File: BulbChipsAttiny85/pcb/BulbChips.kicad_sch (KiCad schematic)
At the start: 27 parts, among them J1 USB_C_Receptacle_USB2.0_14P, SW1 SW_Push, U1 DMN52D0UV, U2 USBLC6-2P6, U3 S-82A1ACA-I6T1U, U4 ATtiny85-20M, U5 BQ24045DSQR

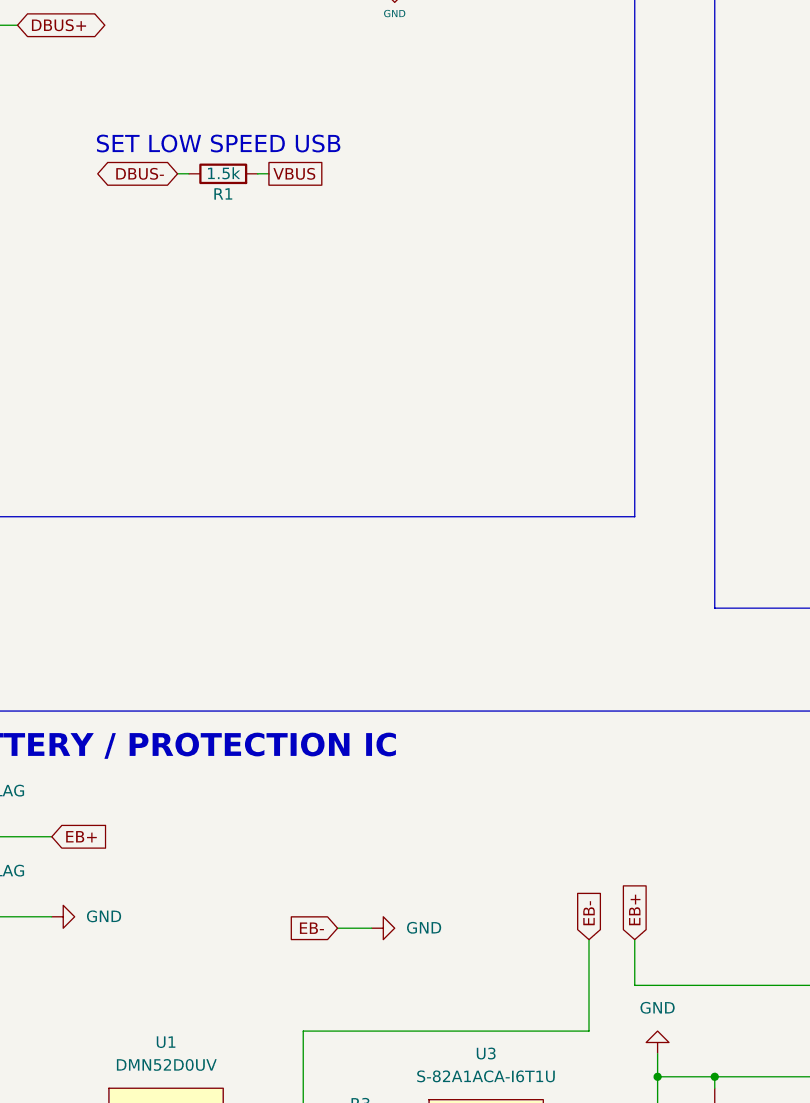
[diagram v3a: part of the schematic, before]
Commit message: changed usb low speed resistor from 1.5k to 2.2k because using 5v from usb, not 3.3v
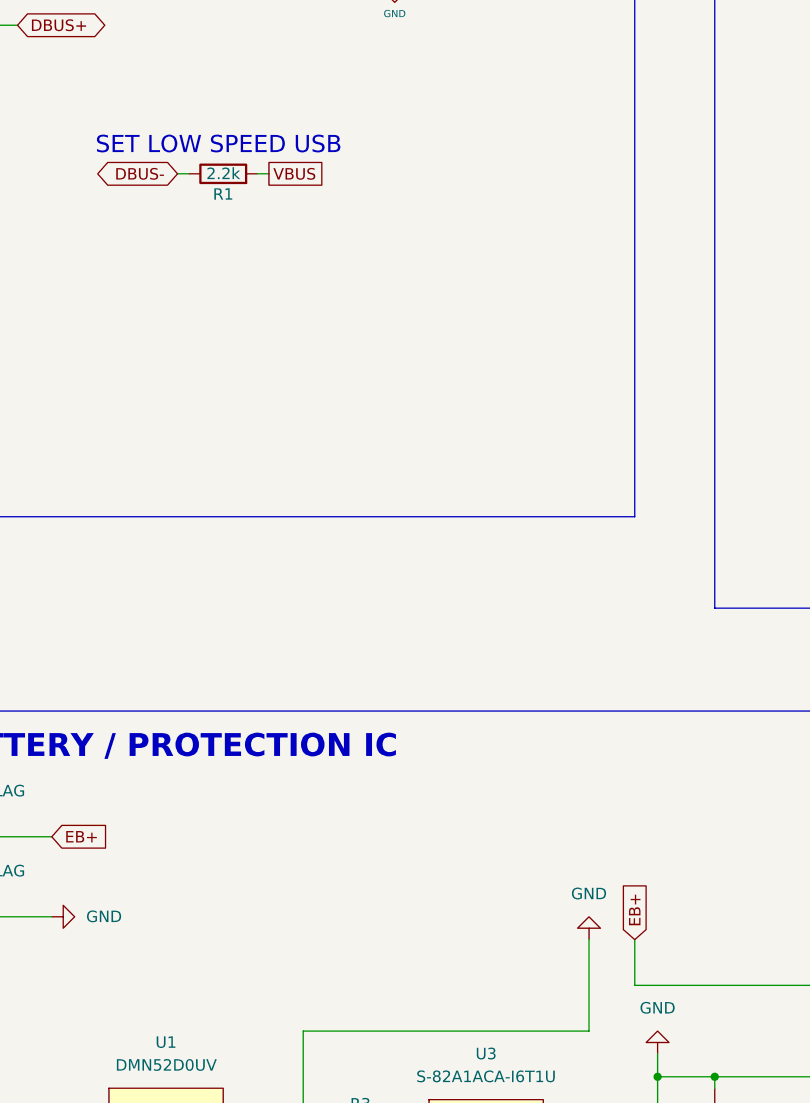
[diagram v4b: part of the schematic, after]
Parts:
- R1: value 1.5k -> 2.2k
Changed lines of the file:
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@@
 	(wire
 		(pts
-			(xy 101.6 240.03) (xy 105.41 240.03)
-		)
-		(stroke
-			(width 0)
-			(type default)
-		)
-	)
-	(wire
-		(pts
 			(xy 261.62 146.05) (xy 261.62 157.48)
 		)
@@
 		)
 	)
-	(global_label "EB-"
-		(shape input)
-		(at 101.6 240.03 180)
-		(fields_autoplaced yes)
-		(effects
-			(font
-				(size 1.27 1.27)
-			)
-			(justify right)
-		)
-		(property "Intersheetrefs" "${INTERSHEET_REFS}"
-			(at 94.6234 240.03 0)
-			(effects
-				(font
-					(size 1.27 1.27)
-				)
-				(justify right)
-				(hide yes)
-			)
-		)
-	)
 	(global_label "Button"
 		(shape passive)
@@
 		)
 	)
-	(global_label "EB-"
-		(shape input)
-		(at 129.54 241.3 90)
-		(fields_autoplaced yes)
-		(effects
-			(font
-				(size 1.27 1.27)
-			)
-			(justify left)
-		)
-		(property "Intersheetrefs" "${INTERSHEET_REFS}"
-			(at 129.54 234.3234 90)
-			(effects
-				(font
-					(size 1.27 1.27)
-				)
-				(justify left)
-				(hide yes)
-			)
-		)
-	)
 	(global_label "D-"
 		(shape bidirectional)
@@
 	(symbol
 		(lib_id "power:GND")
+		(at 129.54 241.3 180)
+		(unit 1)
+		(exclude_from_sim no)
+		(in_bom yes)
+		(on_board yes)
+		(dnp no)
+		(fields_autoplaced yes)
+		(property "Reference" "#PWR04"
+			(at 129.54 234.95 0)
+			(effects
+				(font
+					(size 1.27 1.27)
+				)
+				(hide yes)
+			)
+		)
+		(property "Value" "GND"
+			(at 129.54 236.22 0)
+			(effects
+				(font
+					(size 1.27 1.27)
+				)
+			)
+		)
+		(property "Footprint" ""
+			(at 129.54 241.3 0)
+			(effects
+				(font
+					(size 1.27 1.27)
+				)
+				(hide yes)
+			)
+		)
+		(property "Datasheet" ""
+			(at 129.54 241.3 0)
+			(effects
+				(font
+					(size 1.27 1.27)
+				)
+				(hide yes)
+			)
+		)
+		(property "Description" "Power symbol creates a global label with name \"GND\" , ground"
+			(at 129.54 241.3 0)
+			(effects
+				(font
+					(size 1.27 1.27)
+				)
+				(hide yes)
+			)
+		)
+		(pin "1"
+		)
+		(instances
+			(project "BulbChips"
+				(path "/fc2915fa-7a9c-445c-a5d7-b7fdeb691e1a"
+					(reference "#PWR04")
+					(unit 1)
+				)
+			)
+		)
+	)
+	(symbol
+		(lib_id "power:GND")
 		(at 287.02 66.04 90)
 		(unit 1)
@@
 	)
 	(symbol
-		(lib_id "power:GND")
-		(at 105.41 240.03 90)
-		(unit 1)
-		(exclude_from_sim no)
-		(in_bom yes)
-		(on_board yes)
-		(dnp no)
-		(fields_autoplaced yes)
-		(property "Reference" "#PWR03"
-			(at 111.76 240.03 0)
-			(effects
-				(font
-					(size 1.27 1.27)
-				)
-				(hide yes)
-			)
-		)
-		(property "Value" "GND"
-			(at 109.22 240.0299 90)
-			(effects
-				(font
-					(size 1.27 1.27)
-				)
-				(justify right)
-			)
-		)
-		(property "Footprint" ""
-			(at 105.41 240.03 0)
-			(effects
-				(font
-					(size 1.27 1.27)
-				)
-				(hide yes)
-			)
-		)
-		(property "Datasheet" ""
-			(at 105.41 240.03 0)
-			(effects
-				(font
-					(size 1.27 1.27)
-				)
-				(hide yes)
-			)
-		)
-		(property "Description" "Power symbol creates a global label with name \"GND\" , ground"
-			(at 105.41 240.03 0)
-			(effects
-				(font
-					(size 1.27 1.27)
-				)
-				(hide yes)
-			)
-		)
-		(pin "1"
-		)
-		(instances
-			(project "BulbChips"
-				(path "/fc2915fa-7a9c-445c-a5d7-b7fdeb691e1a"
-					(reference "#PWR03")
-					(unit 1)
-				)
-			)
-		)
-	)
-	(symbol
 		(lib_id "power:PWR_FLAG")
 		(at 62.23 229.87 0)
@@
 		(on_board yes)
 		(dnp no)
-		(property "Reference" "#PWR04"
+		(property "Reference" "#PWR03"
 			(at 107.95 140.97 0)
 			(effects
@@
 			(project "BulbChips"
 				(path "/fc2915fa-7a9c-445c-a5d7-b7fdeb691e1a"
-					(reference "#PWR04")
+					(reference "#PWR03")
 					(unit 1)
 				)
@@
 			)
 		)
-		(property "Value" "1.5k"
+		(property "Value" "2.2k"
 			(at 88.9 156.21 90)
 			(effects

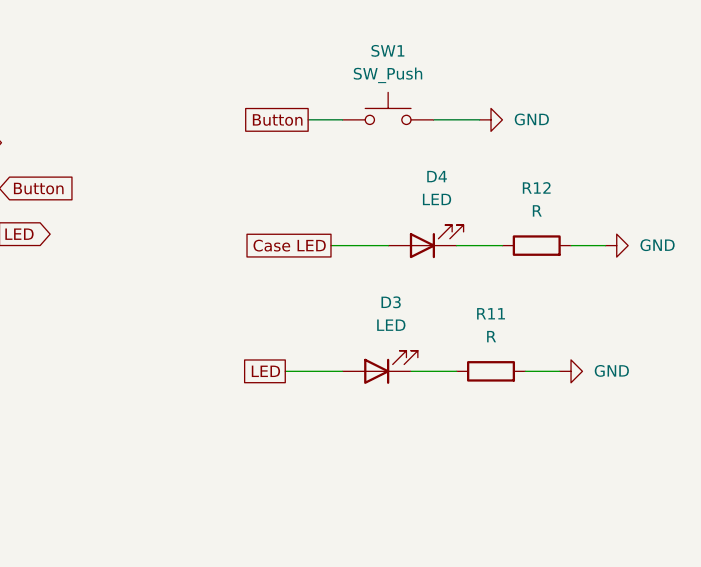
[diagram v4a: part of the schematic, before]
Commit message: added 0603 size for all resistors and capacitors, switched main led out for 2 pin socket
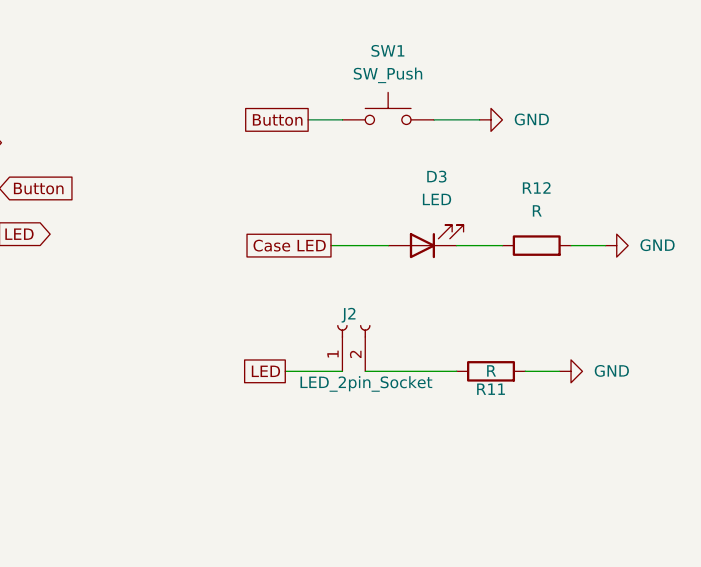
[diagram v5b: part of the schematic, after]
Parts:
- removed D3: LED, symbol Device:LED
- added J2: LED_2pin_Socket, Connector_PinHeader_2.54mm:PinHeader_1x02_P2.54mm_Vertical_SMD_Pin1Right, symbol Connector:Conn_01x02_Socket
- C1, C2, C3: footprint (none) -> Capacitor_SMD:C_0201_0603Metric
- D1, D2: footprint (none) -> LED_SMD:LED_0201_0603Metric
- D3: renamed from D4; footprint (none) -> LED_SMD:LED_0201_0603Metric
- R1, R10, R11, R12, R2, R3, R4, R5, R6, R7, R8, R9: footprint (none) -> Resistor_SMD:R_0201_0603Metric
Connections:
- net LED: now also J2.1 (Pin_1)
- net at R11.1: now also J2.2 (Pin_2)
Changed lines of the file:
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@@
 	(wire
 		(pts
+			(xy 274.32 93.98) (xy 284.48 93.98)
+		)
+		(stroke
+			(width 0)
+			(type default)
+		)
+	)
+	(wire
+		(pts
 			(xy 176.53 91.44) (xy 204.47 91.44)
 		)
@@
 	(wire
 		(pts
-			(xy 279.4 93.98) (xy 284.48 93.98)
-		)
-		(stroke
-			(width 0)
-			(type default)
-		)
-	)
-	(wire
-		(pts
 			(xy 260.35 157.48) (xy 261.62 157.48)
 		)
@@
 			)
 		)
-		(property "Footprint" ""
+		(property "Footprint" "Resistor_SMD:R_0201_0603Metric"
 			(at 180.34 157.988 90)
 			(effects
@@
 			)
 		)
-		(property "Footprint" ""
+		(property "Footprint" "Capacitor_SMD:C_0201_0603Metric"
 			(at 201.6252 152.4 0)
 			(effects
@@
 			)
 		)
-		(property "Footprint" ""
+		(property "Footprint" "Resistor_SMD:R_0201_0603Metric"
 			(at 180.34 166.878 90)
 			(effects
@@
 			)
 		)
-		(property "Footprint" ""
+		(property "Footprint" "Resistor_SMD:R_0201_0603Metric"
 			(at 104.14 263.398 90)
 			(effects
@@
 		(on_board yes)
 		(dnp no)
-		(fields_autoplaced yes)
 		(property "Reference" "R11"
-			(at 288.29 87.63 90)
+			(at 288.29 96.012 90)
 			(effects
 				(font
@@
 		)
 		(property "Value" "R"
-			(at 288.29 90.17 90)
+			(at 288.29 93.98 90)
 			(effects
 				(font
@@
 			)
 		)
-		(property "Footprint" ""
+		(property "Footprint" "Resistor_SMD:R_0201_0603Metric"
 			(at 288.29 95.758 90)
 			(effects
@@
 			)
 		)
-		(property "Footprint" ""
+		(property "Footprint" "Resistor_SMD:R_0201_0603Metric"
 			(at 256.54 159.258 90)
 			(effects
@@
 			)
 		)
-		(property "Footprint" ""
+		(property "Footprint" "Resistor_SMD:R_0201_0603Metric"
 			(at 151.13 271.018 90)
 			(effects
@@
 		(on_board yes)
 		(dnp no)
-		(property "Reference" "D4"
+		(property "Reference" "D3"
 			(at 282.2575 72.39 0)
 			(effects
@@
 			)
 		)
-		(property "Footprint" ""
+		(property "Footprint" "LED_SMD:LED_0201_0603Metric"
 			(at 280.67 80.01 0)
 			(effects
@@
 			(project "BulbChips"
 				(path "/fc2915fa-7a9c-445c-a5d7-b7fdeb691e1a"
-					(reference "D4")
+					(reference "D3")
 					(unit 1)
 				)
@@
 	)
 	(symbol
+		(lib_id "Connector:Conn_01x02_Socket")
+		(at 271.78 88.9 90)
+		(unit 1)
+		(exclude_from_sim no)
+		(in_bom yes)
+		(on_board yes)
+		(dnp no)
+		(property "Reference" "J2"
+			(at 271.78 87.63 90)
+			(effects
+				(font
+					(size 1.27 1.27)
+				)
+				(justify right)
+			)
+		)
+		(property "Value" "LED_2pin_Socket"
+			(at 266.954 95.25 90)
+			(effects
+				(font
+					(size 1.27 1.27)
+				)
+				(justify right)
+			)
+		)
+		(property "Footprint" "Connector_PinHeader_2.54mm:PinHeader_1x02_P2.54mm_Vertical_SMD_Pin1Right"
+			(at 271.78 88.9 0)
+			(effects
+				(font
+					(size 1.27 1.27)
+				)
+				(hide yes)
+			)
+		)
+		(property "Datasheet" "~"
+			(at 271.78 88.9 0)
+			(effects
+				(font
+					(size 1.27 1.27)
+				)
+				(hide yes)
+			)
+		)
+		(property "Description" "Generic connector, single row, 01x02, script generated"
+			(at 271.78 88.9 0)
+			(effects
+				(font
+					(size 1.27 1.27)
+				)
+				(hide yes)
+			)
+		)
+		(pin "1"
+		)
+		(pin "2"
+		)
+		(instances
+			(project ""
+				(path "/fc2915fa-7a9c-445c-a5d7-b7fdeb691e1a"
+					(reference "J2")
+					(unit 1)
+				)
+			)
+		)
+	)
+	(symbol
 		(lib_id "BulbLib:DMN52D0UV")
 		(at 82.55 259.08 0)
@@
 			)
 		)
-		(property "Footprint" ""
+		(property "Footprint" "Resistor_SMD:R_0201_0603Metric"
 			(at 293.37 81.788 90)
 			(effects
@@
 			)
 		)
-		(property "Footprint" ""
+		(property "Footprint" "LED_SMD:LED_0201_0603Metric"
 			(at 248.92 146.05 0)
 			(effects
@@
 			)
 		)
-		(property "Footprint" ""
+		(property "Footprint" "LED_SMD:LED_0201_0603Metric"
 			(at 248.92 157.48 0)
 			(effects
@@
 			)
 		)
-		(property "Footprint" ""
+		(property "Footprint" "Resistor_SMD:R_0201_0603Metric"
 			(at 97.79 135.128 90)
 			(effects
@@
 			)
 		)
-		(property "Footprint" ""
+		(property "Footprint" "Resistor_SMD:R_0201_0603Metric"
 			(at 256.54 147.828 90)
 			(effects
@@
 	)
 	(symbol
-		(lib_id "Device:LED")
-		(at 275.59 93.98 180)
-		(unit 1)
-		(exclude_from_sim no)
-		(in_bom yes)
-		(on_board yes)
-		(dnp no)
-		(property "Reference" "D3"
-			(at 277.1775 86.36 0)
-			(effects
-				(font
-					(size 1.27 1.27)
-				)
-			)
-		)
-		(property "Value" "LED"
-			(at 277.1775 88.9 0)
-			(effects
-				(font
-					(size 1.27 1.27)
-				)
-			)
-		)
-		(property "Footprint" ""
-			(at 275.59 93.98 0)
-			(effects
-				(font
-					(size 1.27 1.27)
-				)
-				(hide yes)
-			)
-		)
-		(property "Datasheet" "~"
-			(at 275.59 93.98 0)
-			(effects
-				(font
-					(size 1.27 1.27)
-				)
-				(hide yes)
-			)
-		)
-		(property "Description" "Light emitting diode"
-			(at 275.59 93.98 0)
-			(effects
-				(font
-					(size 1.27 1.27)
-				)
-				(hide yes)
-			)
-		)
-		(pin "2"
-		)
-		(pin "1"
-		)
-		(instances
-			(project ""
-				(path "/fc2915fa-7a9c-445c-a5d7-b7fdeb691e1a"
-					(reference "D3")
-					(unit 1)
-				)
-			)
-		)
-	)
-	(symbol
 		(lib_id "Switch:SW_Push")
 		(at 276.86 66.04 0)
@@
 			)
 		)
-		(property "Footprint" ""
+		(property "Footprint" "Capacitor_SMD:C_0201_0603Metric"
 			(at 144.4752 265.43 0)
 			(effects
@@
 			)
 		)
-		(property "Footprint" ""
+		(property "Footprint" "Capacitor_SMD:C_0201_0603Metric"
 			(at 177.4952 91.44 0)
 			(effects
@@
 			)
 		)
-		(property "Footprint" ""
+		(property "Footprint" "Resistor_SMD:R_0201_0603Metric"
 			(at 88.9 157.988 90)
 			(effects
@@
 			)
 		)
-		(property "Footprint" ""
+		(property "Footprint" "Resistor_SMD:R_0201_0603Metric"
 			(at 118.11 131.572 90)
 			(effects
@@
 			)
 		)
-		(property "Footprint" ""
+		(property "Footprint" "Resistor_SMD:R_0201_0603Metric"
 			(at 133.35 268.478 90)
 			(effects

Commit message: organization and labeling
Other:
- note added: "MCU"
- note added: "USER EXPERIENCE"
- moved on the sheet: BT1, C1, C2, C3, D1, D2, D3, J1, J2, R1, R10, R11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
